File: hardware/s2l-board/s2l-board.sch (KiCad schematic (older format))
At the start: 61 parts, among them J1 To XLR3-M input, J2 To motherboard, J3 From PSU, U1 LM741, U2 LM741, U3 LM741, U4 LM741, U5 LM741

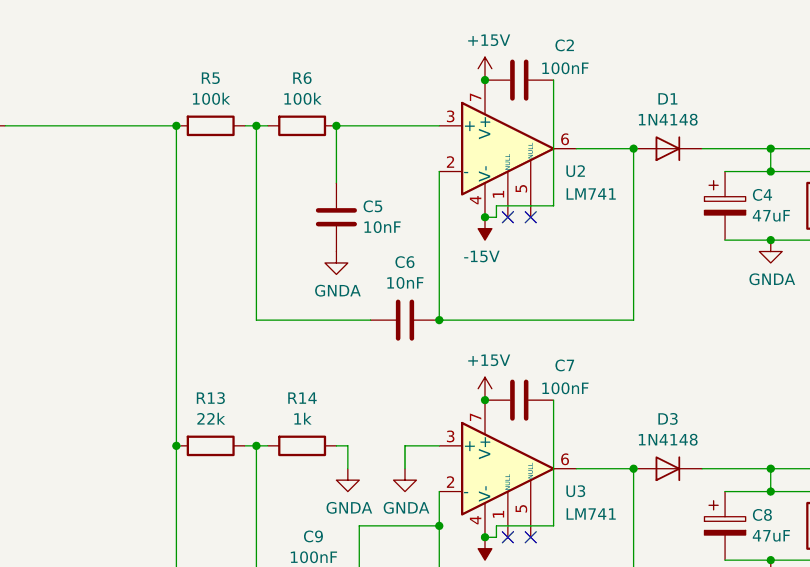
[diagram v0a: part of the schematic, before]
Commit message: Sound to light board completed, PSU board completed
Rev As as ordered
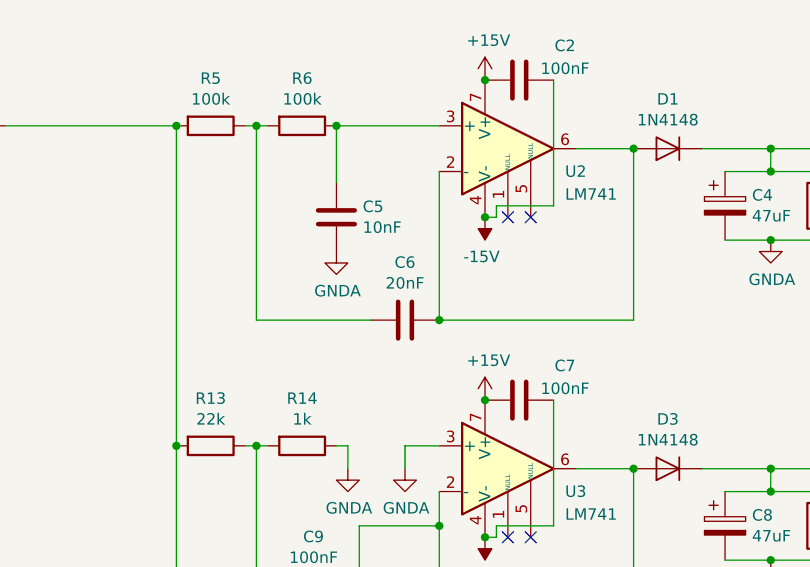
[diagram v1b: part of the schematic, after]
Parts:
- C1, C11, C15, C2, C7: footprint (none) -> Capacitor_THT:C_Disc_D5.0mm_W2.5mm_P5.00mm
- C10, C13, C14, C17, C18, C9: footprint (none) -> Capacitor_THT:C_Rect_L7.2mm_W4.5mm_P5.00mm_FKS2_FKP2_MKS2_MKP2
- C12, C16, C4, C8: footprint (none) -> Capacitor_THT:CP_Radial_D4.0mm_P1.50mm
- C3: footprint (none) -> Capacitor_THT:C_Disc_D3.0mm_W2.0mm_P2.50mm
- C5: footprint (none) -> Capacitor_THT:C_Rect_L7.0mm_W2.5mm_P5.00mm
- C6: value 10nF -> 20nF; footprint (none) -> Capacitor_THT:C_Rect_L7.2mm_W2.5mm_P5.00mm_FKS2_FKP2_MKS2_MKP2
- D1, D2, D3, D4, D5, D6, D7, D8: footprint (none) -> Diode_THT:D_DO-35_SOD27_P7.62mm_Horizontal
- J1, J2, J3: footprint (none) -> Connector_PinHeader_2.54mm:Molex_KK254_1x04Vertical
- R1, R10, R11, R12, R13, R14, R15, R16, R17, R18, R19, R2, R20, R21, R22, R23, R24, R25, R26, R27, R3, R4, R5, R6, R7, R8, R9: footprint (none) -> Resistor_THT:R_Axial_DIN0207_L6.3mm_D2.5mm_P10.16mm_Horizontal
- U1, U2, U3, U4, U5: footprint (none) -> Package_DIP:DIP-8_W7.62mm_Socket
